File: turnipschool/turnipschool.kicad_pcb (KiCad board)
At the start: 4 copper layers, 22.5 x 12 mm, 61 parts, among them J1 USB-DEVICE-SHIELD, P1 CONN_1, P2 RESET_N, P3 DD, P4 DC, P5 3V3, P6 GND, P7 CABLE, T1 BALUN, U1 CC1111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

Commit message: removed thermals under QFNs
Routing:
- net GND: track 48.5 -> 79.3 mm
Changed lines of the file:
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@@
     (thickness 1.6002)
     (drawings 20)
-    (tracks 584)
+    (tracks 597)
     (zones 0)
     (modules 61)
@@
   )
   (setup
-    (last_trace_width 0.2286)
+    (last_trace_width 1.27)
     (user_trace_width 0.2286)
     (user_trace_width 0.508)
@@
   (segment (start 108.9366 90.57) (end 108.36 90.57) (width 0.2286) (layer C1F) (net 8))
   (segment (start 109.0666 90.7) (end 108.9366 90.57) (width 0.2286) (layer C1F) (net 8))
+  (segment (start 98 91) (end 100 93) (width 1.27) (layer C2) (net 9))
+  (segment (start 98 93) (end 98 91) (width 1.27) (layer C2) (net 9))
+  (segment (start 100 93) (end 98 93) (width 1.27) (layer C2) (net 9))
+  (segment (start 100 91) (end 100 93) (width 1.27) (layer C2) (net 9))
+  (segment (start 98 91) (end 100 91) (width 1.27) (layer C2) (net 9))
+  (segment (start 103.0395 91.4605) (end 105.9605 88.5395) (width 1.27) (layer C2) (net 9))
+  (segment (start 105.9605 88.5395) (end 105.96 88.54) (width 1.27) (layer C2) (net 9))
+  (segment (start 105.96 88.54) (end 105.9605 88.5395) (width 1.27) (layer C2) (net 9))
+  (segment (start 103.0395 88.5395) (end 105.9605 91.4605) (width 1.27) (layer C2) (net 9))
+  (segment (start 103.0395 91.4605) (end 103.0395 88.5395) (width 1.27) (layer C2) (net 9))
+  (segment (start 105.9605 91.4605) (end 103.0395 91.4605) (width 1.27) (layer C2) (net 9))
+  (segment (start 105.9605 88.5395) (end 105.9605 91.4605) (width 1.27) (layer C2) (net 9))
+  (segment (start 103.0395 88.5395) (end 105.9605 88.5395) (width 1.27) (layer C2) (net 9))
   (segment (start 109.9534 88.4) (end 109.99 88.4366) (width 0.2286) (layer C4B) (net 9))
   (segment (start 109.99 88.4366) (end 109.99 89.0566) (width 0.2286) (layer C4B) (net 9))

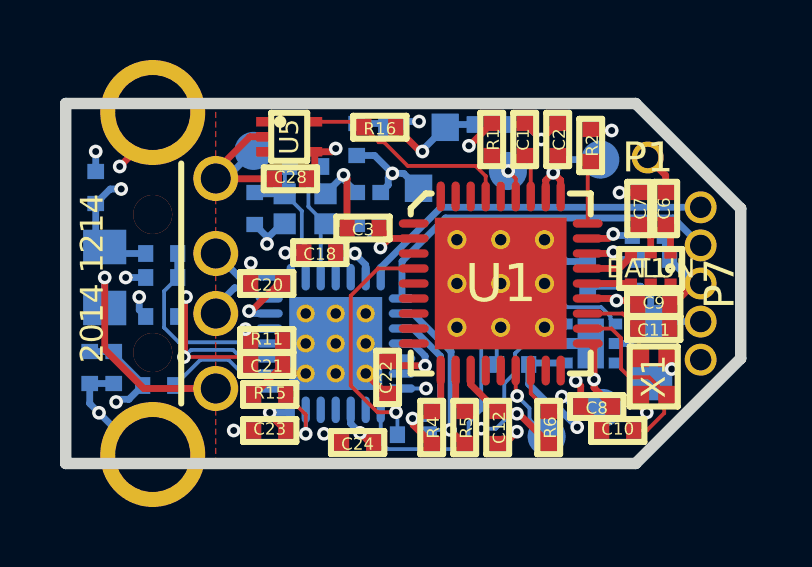
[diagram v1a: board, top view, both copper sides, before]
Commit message: updated date on silkscreen
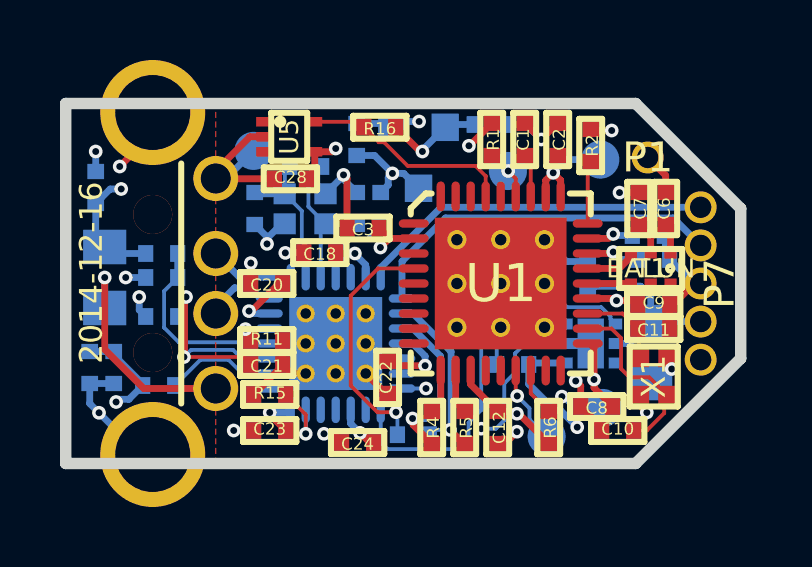
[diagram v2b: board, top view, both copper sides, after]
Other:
- board text added: "2014-12-16"
- board text removed: "2014 1214"
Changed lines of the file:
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@@
     (effects (font (size 0.6096 0.6096) (thickness 0.127)) (justify mirror))
   )
-  (gr_text "2014 1214" (at 90.88 89.83 90) (layer F.SilkS)
+  (gr_text 2014-12-16 (at 90.85 89.64 90) (layer F.SilkS)
     (effects (font (size 0.762 0.762) (thickness 0.1524)))
   )

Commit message: moved magnetic sensor to DC pin
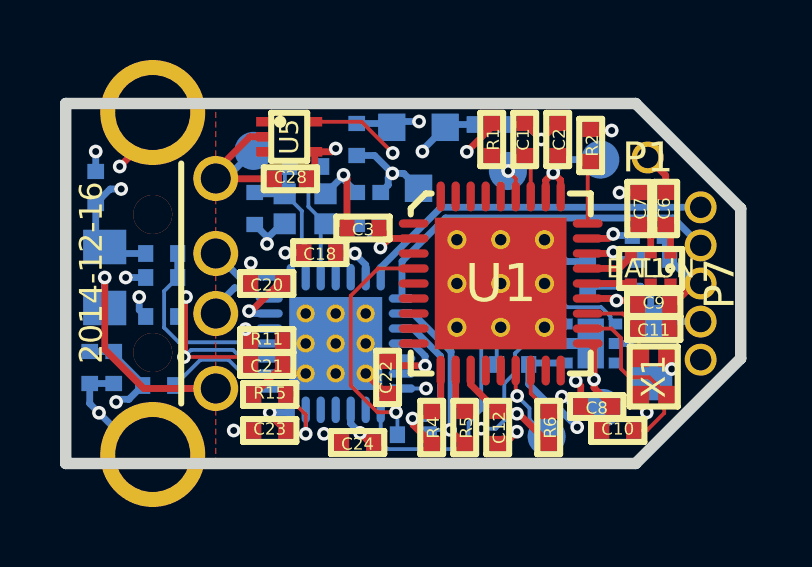
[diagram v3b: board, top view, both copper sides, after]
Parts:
- removed R16: 10k, cc1111-legacy:GSG-0402
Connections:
- U1 pad 33: Net-(R16-Pad1) -> (no net)
- U5 pad 5: Net-(R16-Pad1) -> /DC
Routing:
- net /DC: track 3.81 -> 23.8 mm, vias 1 -> 2
- net Net-(R16-Pad1): track 7.59 -> 0.00 mm
- net 3V3: track 39.9 -> 38.9 mm

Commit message: updated date on silkscreen
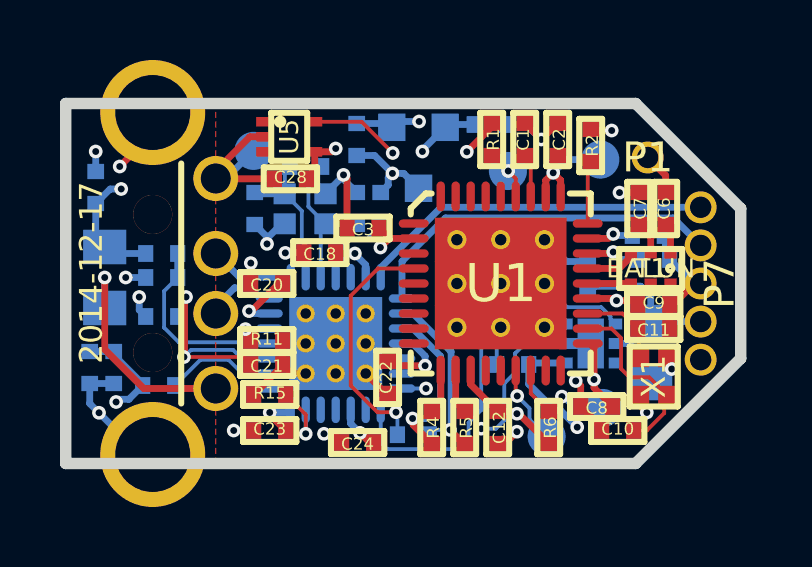
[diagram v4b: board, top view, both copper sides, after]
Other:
- board text added: "2014-12-17"
- board text removed: "2014-12-16"
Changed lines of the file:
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@@
     (links 171)
     (no_connects 0)
-    (area 89.809499 83.809499 112.690501 96.190501)
+    (area 75.098399 82.048399 123.301601 97.951601)
     (thickness 1.6002)
     (drawings 20)
@@
     (effects (font (size 0.6096 0.6096) (thickness 0.127)) (justify mirror))
   )
-  (gr_text 2014-12-16 (at 90.85 89.64 90) (layer F.SilkS)
+  (gr_text 2014-12-17 (at 90.85 89.64 90) (layer F.SilkS)
     (effects (font (size 0.762 0.762) (thickness 0.1524)))
   )

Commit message: reworked layout so USB traces have contiguous zones beneath them
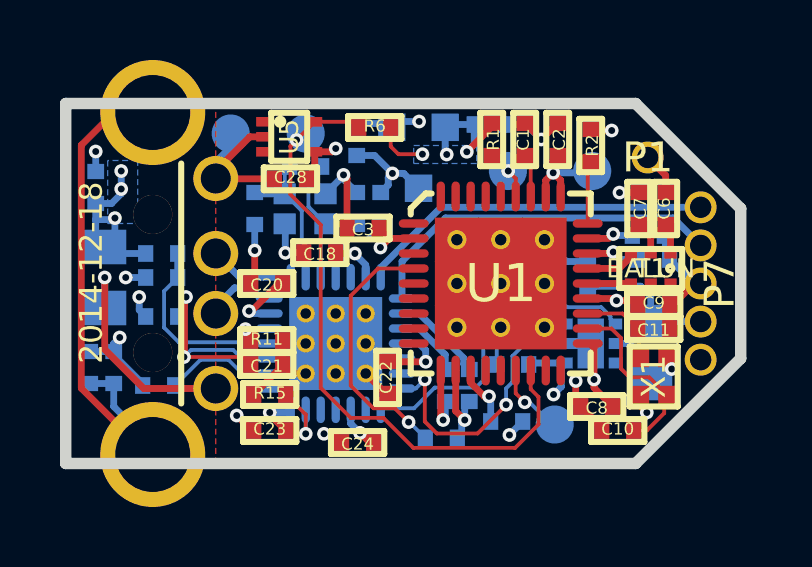
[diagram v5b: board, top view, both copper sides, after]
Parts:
- C12, R4, R5: moved to B.Cu
- moved P4 13.5 mm to (98.0, 85.0)
- moved R6 11.6 mm to (100.3, 84.8), turned to 180 degrees
- moved R4 1.47 mm to (102.7, 93.4), turned to 270 degrees
- moved R5 1.41 mm to (103.5, 93.4), turned to 270 degrees
- moved P6 0.96 mm to (95.5, 85.0)
- moved R17 0.94 mm to (102.5, 95.2)
- moved P3 0.48 mm to (106.3, 94.7)
- moved P5 0.47 mm to (107.5, 86.2)
- moved C12 0.36 mm to (104.7, 94.6), turned to 180 degrees
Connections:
- R5 pad 1: Net-(R17-Pad1) -> Net-(R5-Pad1)
- R5 pad 2: Net-(R5-Pad2) -> Net-(R17-Pad1)
- U1 pad 11: Net-(R5-Pad2) -> Net-(R17-Pad1)
- U3 pad 2: Net-(R17-Pad1) -> Net-(R5-Pad1)
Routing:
- net GND: track 79.3 -> 91.8 mm, vias 17 -> 16
- net /SHIELD: track 26.7 -> 38.1 mm, vias 2 -> 0
- net Net-(R5-Pad1): track 0.00 -> 3.30 mm
- net Net-(R17-Pad1): track 6.44 -> 3.33 mm
- net Net-(R4-Pad1): track 5.70 -> 2.89 mm, vias 1 -> 0
- net Net-(U3-Pad8): track 13.5 -> 11.1 mm
- net Net-(R5-Pad2): track 1.49 -> 0.00 mm
- net /VBUS: track 10.4 -> 11.4 mm, vias 3 -> 5
- net /DD: track 2.63 -> 3.55 mm
- net Net-(U3-Pad7): track 9.31 -> 10.2 mm
- net Net-(R4-Pad2): track 1.49 -> 2.33 mm, vias 0 -> 1
- net Net-(R17-Pad2): track 8.19 -> 8.88 mm
- net /DC: track 23.8 -> 23.3 mm, vias 2 -> 1
- net 3V3: track 38.9 -> 39.4 mm, vias 16 -> 17
- added copper zone on C2, net /SHIELD
- added copper zone on B.Cu, net /VBUS
- added copper zone on B.Cu, net 3V3
- removed copper zone on C3, net /SHIELD
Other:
- board text added: "2014-12-18"
- board text removed: "2014-12-17"

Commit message: corrected USB connector BOM info
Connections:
- U1 pad 1: (no net) -> Net-(U1-Pad1)
- U1 pad 13: (no net) -> Net-(U1-Pad13)
- U1 pad 14: (no net) -> Net-(U1-Pad14)
- U1 pad 17: (no net) -> Net-(U1-Pad17)
- U1 pad 18: (no net) -> Net-(U1-Pad18)
- U1 pad 3: (no net) -> Net-(U1-Pad3)
- U1 pad 32: (no net) -> Net-(U1-Pad32)
- U1 pad 33: (no net) -> Net-(U1-Pad33)
- U1 pad 34: (no net) -> Net-(U1-Pad34)
- U1 pad 35: (no net) -> Net-(U1-Pad35)
- U1 pad 36: (no net) -> Net-(U1-Pad36)
- U1 pad 5: (no net) -> Net-(U1-Pad5)
- U1 pad 6: (no net) -> Net-(U1-Pad6)
- U1 pad 7: (no net) -> Net-(U1-Pad7)
- U1 pad 8: (no net) -> Net-(U1-Pad8)
- U1 pad 9: (no net) -> Net-(U1-Pad9)
- U3 pad 11: (no net) -> Net-(U3-Pad11)
- U3 pad 12: (no net) -> Net-(U3-Pad12)
- U3 pad 25: (no net) -> Net-(U3-Pad25)
- U3 pad 5: (no net) -> Net-(U3-Pad5)
- U3 pad 6: (no net) -> Net-(U3-Pad6)
- U3 pad 9: (no net) -> Net-(U3-Pad9)
- U4 pad 6: (no net) -> Net-(U4-Pad6)
- U5 pad 1: (no net) -> Net-(U5-Pad1)
- U5 pad 3: (no net) -> Net-(U5-Pad3)

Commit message: changed R6 from 10k to 100k for improved reliability of magnetic sensor bootloader activation
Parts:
- R6: value 10k -> 100k

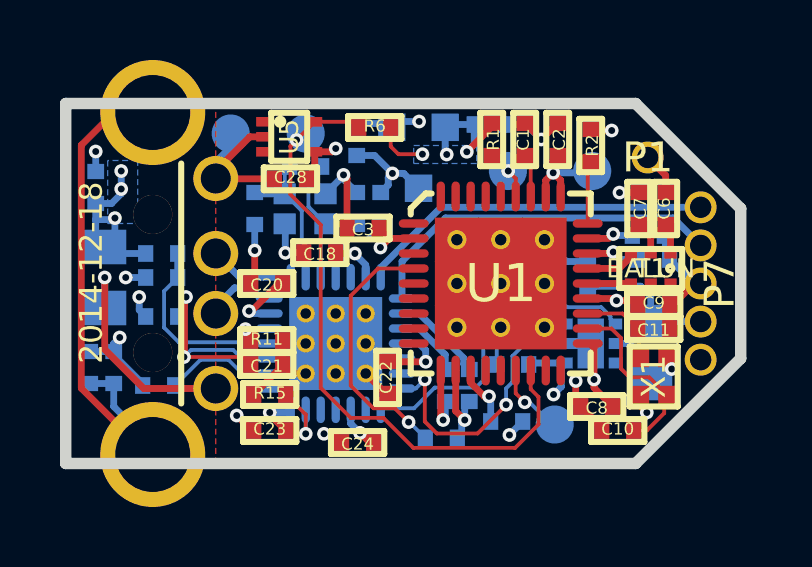
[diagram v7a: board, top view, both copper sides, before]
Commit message: moved R17 from DM to DP
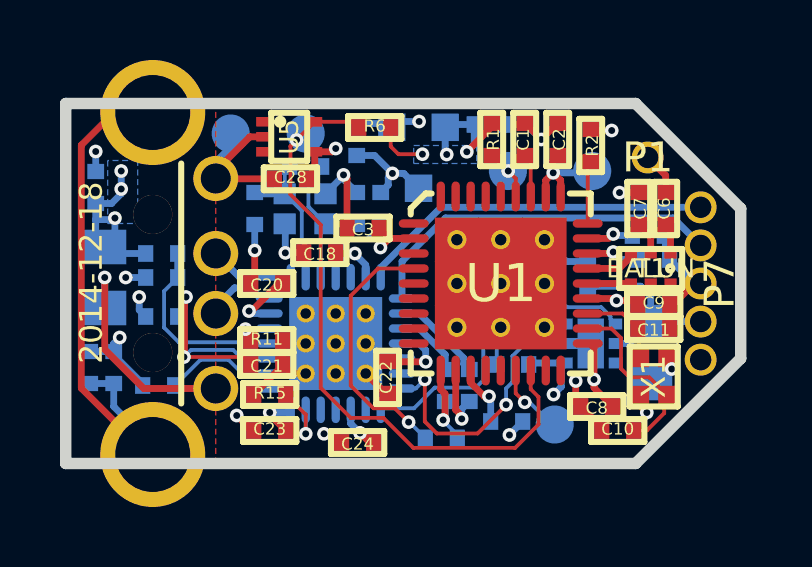
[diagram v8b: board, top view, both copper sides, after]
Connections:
- R4 pad 2: Net-(R4-Pad2) -> Net-(R17-Pad1)
- R5 pad 2: Net-(R17-Pad1) -> Net-(R5-Pad2)
- U1 pad 10: Net-(R4-Pad2) -> Net-(R17-Pad1)
- U1 pad 11: Net-(R17-Pad1) -> Net-(R5-Pad2)
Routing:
- net Net-(R5-Pad2): track 0.00 -> 2.43 mm, vias 0 -> 1
- net Net-(R4-Pad2): track 2.33 -> 0.00 mm, vias 1 -> 0
